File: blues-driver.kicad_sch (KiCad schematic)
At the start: 100 parts, among them Q5 LS844, Q6 BC858C, Q7 LS844, Q8 BC858C, Q9 BC848C, SW2 SW_DPDT_x2, SW3 SW_DIP_SPDT_2pos, U5 TLV9352, U6 TLV9352

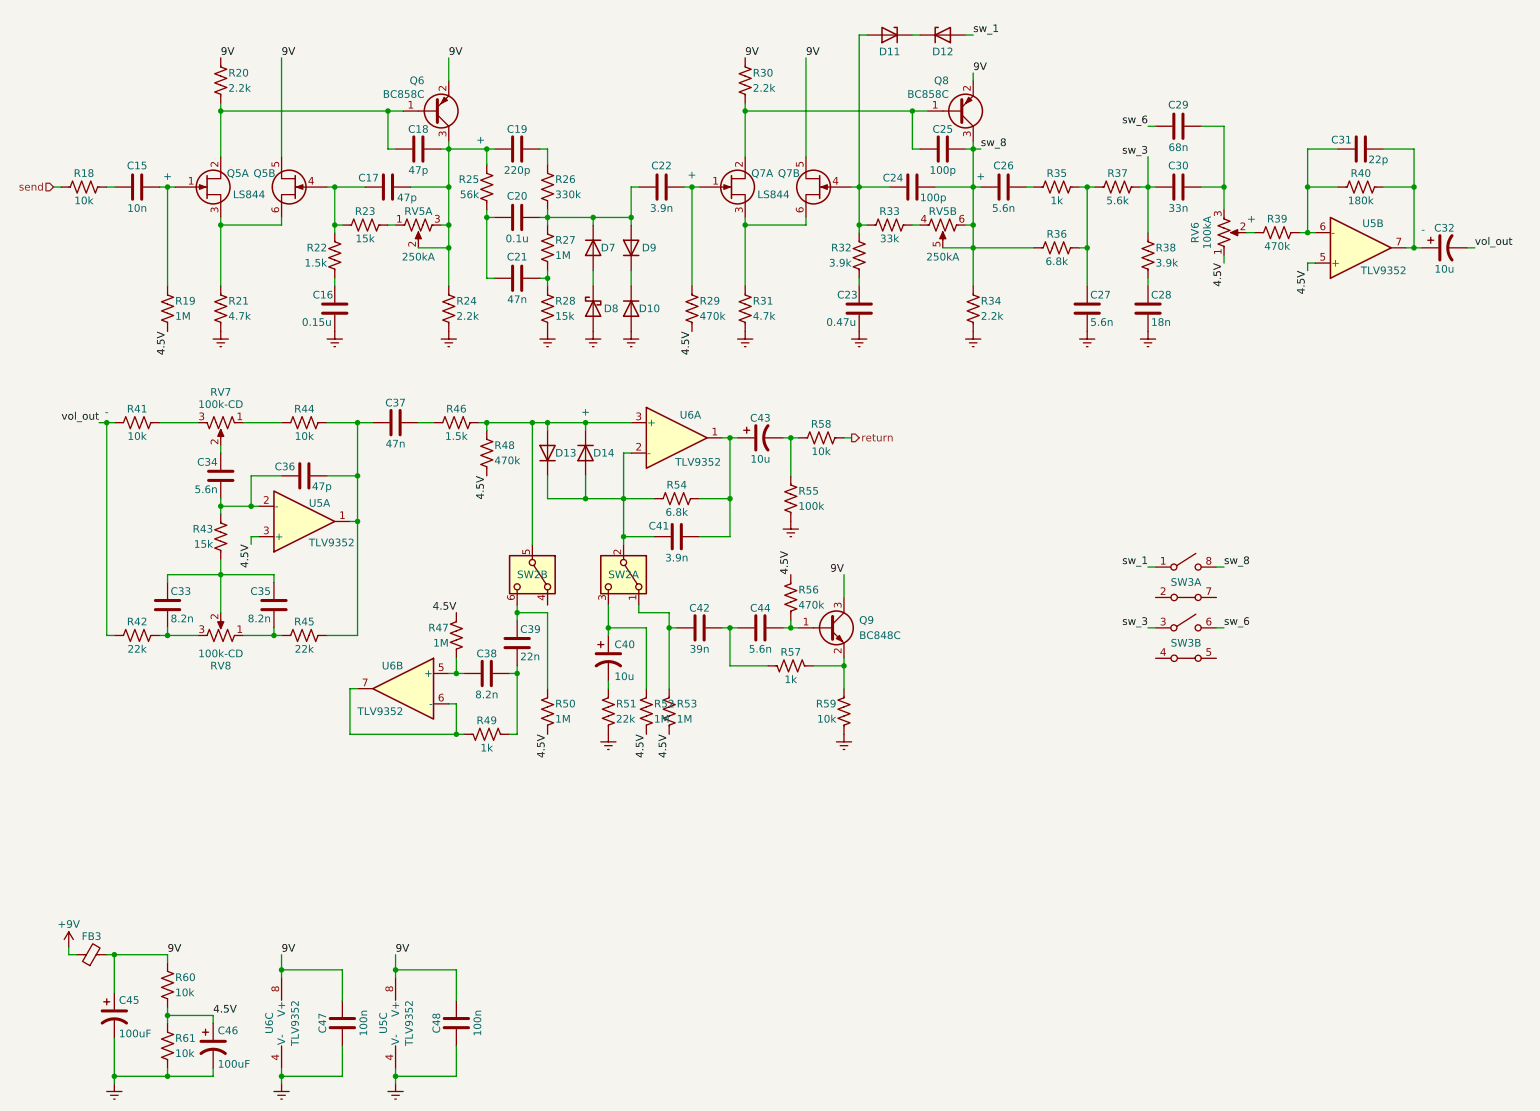
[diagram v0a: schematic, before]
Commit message: finished schematics, started PCB
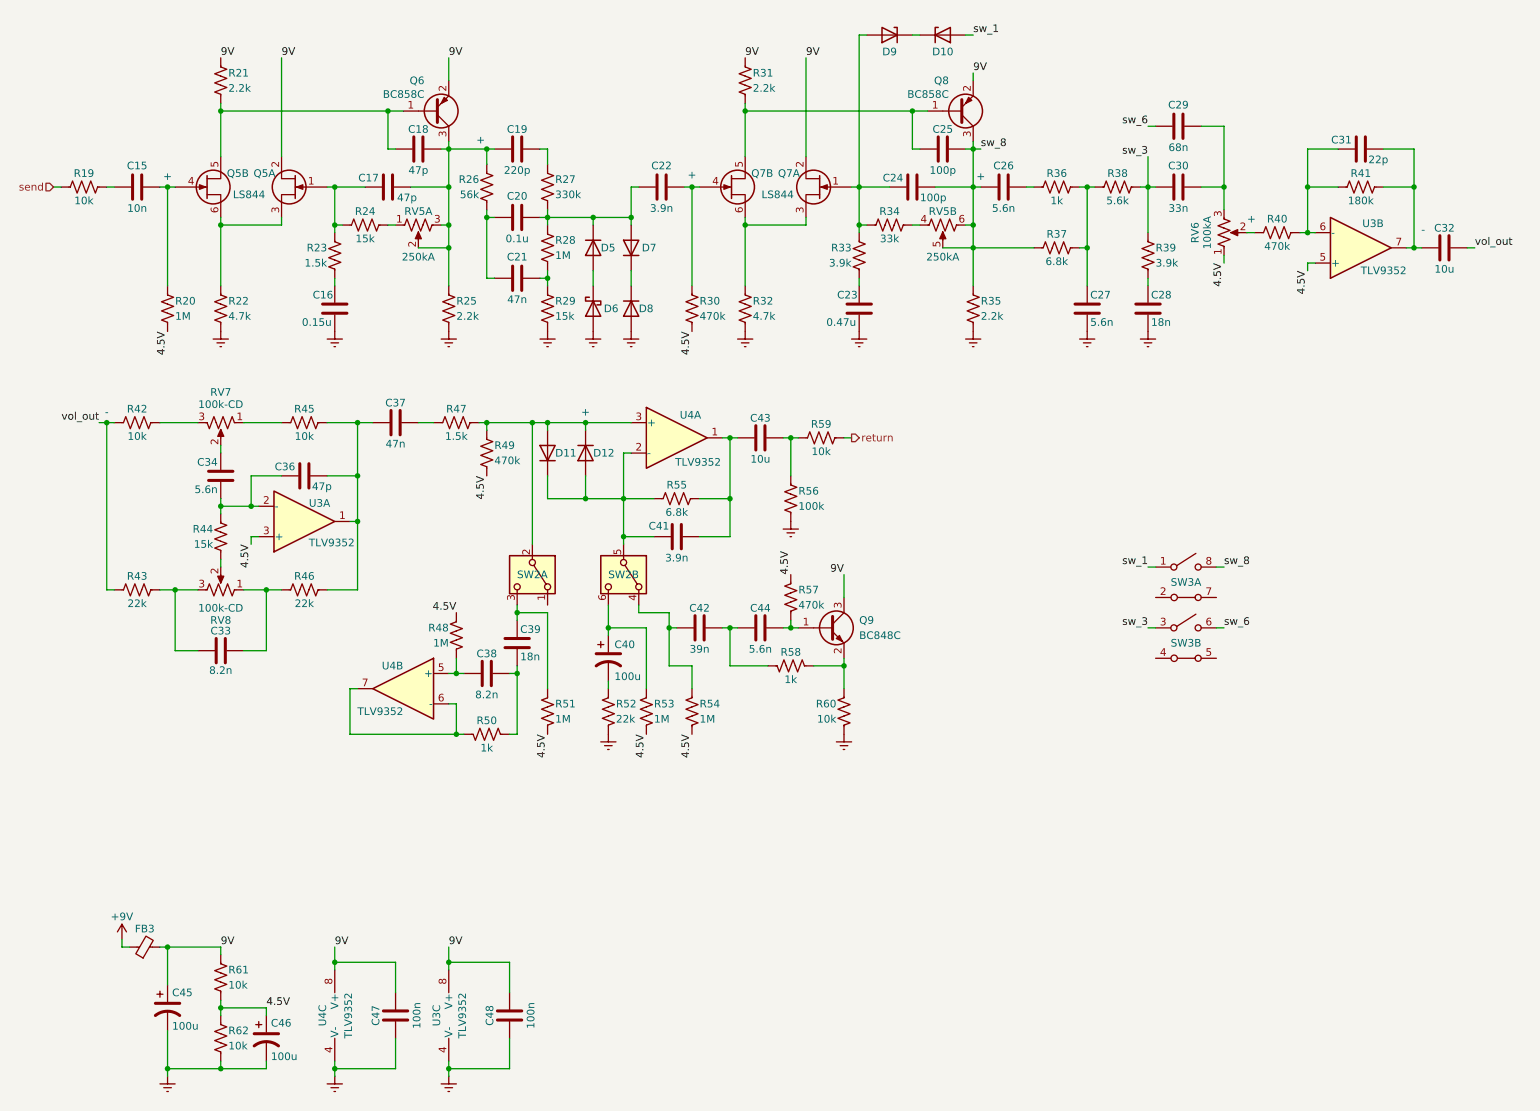
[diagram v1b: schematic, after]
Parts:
- removed C35: 8.2n, bca-footprints:C_Film_L7.2mm_W2.5mm_P5.00mm, symbol bca-symbols:C_Film_W2.50mm
- C17, C18, C24, C25, C31, C36, C47, C48: footprint bca-footprints:C_Ceramic_L4.0mm_W2.5mm_P2.50mm -> Capacitor_SMD:C_0805_2012Metric_Pad1.18x1.45mm_HandSolder
- C32, C43: footprint bca-footprints:CP_Radial_D4.0mm_P1.50mm -> Capacitor_SMD:C_0805_2012Metric_Pad1.18x1.45mm_HandSolder; symbol bca-symbols:CP_Audio -> bca-symbols:C_Ceramic
- C39: value 22n -> 18n
- C40: value 10u -> 100u; footprint bca-footprints:CP_Radial_D4.0mm_P1.50mm -> bca-footprints:CP_Radial_D6.3mm_P2.50mm; symbol bca-symbols:CP_Audio -> bca-symbols:CP_Power
- C45, C46: value 100uF -> 100u
- D10: renamed from D12; footprint (none) -> Diode_SMD:D_SOD-323_HandSoldering
- D11: renamed from D13; footprint (none) -> Diode_SMD:D_SOD-323_HandSoldering
- D12: renamed from D14; footprint (none) -> Diode_SMD:D_SOD-323_HandSoldering
- D5: renamed from D7; footprint (none) -> Diode_SMD:D_SOD-323_HandSoldering
- D6: renamed from D8; footprint (none) -> Diode_SMD:D_SOD-323_HandSoldering
- D7: renamed from D9; footprint (none) -> Diode_SMD:D_SOD-323_HandSoldering
- D8: renamed from D10; footprint (none) -> Diode_SMD:D_SOD-323_HandSoldering
- D9: renamed from D11; footprint (none) -> Diode_SMD:D_SOD-323_HandSoldering
- Q6, Q8, Q9: footprint (none) -> Package_TO_SOT_SMD:SOT-23_Handsoldering
- R20: renamed from R19; footprint bca-footprints:R_L3.6mm_D1.6mm_P5.00mm_Horizontal -> Resistor_SMD:R_0805_2012Metric_Pad1.20x1.40mm_HandSolder
- R21: renamed from R20; footprint bca-footprints:R_L3.6mm_D1.6mm_P5.00mm_Horizontal -> Resistor_SMD:R_0603_1608Metric_Pad0.98x0.95mm_HandSolder
- R22: renamed from R21; footprint bca-footprints:R_L3.6mm_D1.6mm_P5.00mm_Horizontal -> Resistor_SMD:R_0603_1608Metric_Pad0.98x0.95mm_HandSolder
- R25: renamed from R24; footprint bca-footprints:R_L3.6mm_D1.6mm_P5.00mm_Horizontal -> Resistor_SMD:R_0603_1608Metric_Pad0.98x0.95mm_HandSolder
- R31: renamed from R30; footprint bca-footprints:R_L3.6mm_D1.6mm_P5.00mm_Horizontal -> Resistor_SMD:R_0603_1608Metric_Pad0.98x0.95mm_HandSolder
- R32: renamed from R31; footprint bca-footprints:R_L3.6mm_D1.6mm_P5.00mm_Horizontal -> Resistor_SMD:R_0603_1608Metric_Pad0.98x0.95mm_HandSolder
- R35: renamed from R34; footprint bca-footprints:R_L3.6mm_D1.6mm_P5.00mm_Horizontal -> Resistor_SMD:R_0603_1608Metric_Pad0.98x0.95mm_HandSolder
- R48: renamed from R47; footprint bca-footprints:R_L3.6mm_D1.6mm_P5.00mm_Horizontal -> Resistor_SMD:R_0805_2012Metric_Pad1.20x1.40mm_HandSolder
- R51: renamed from R50; footprint bca-footprints:R_L3.6mm_D1.6mm_P5.00mm_Horizontal -> Resistor_SMD:R_0805_2012Metric_Pad1.20x1.40mm_HandSolder
- R53: renamed from R52; footprint bca-footprints:R_L3.6mm_D1.6mm_P5.00mm_Horizontal -> Resistor_SMD:R_0805_2012Metric_Pad1.20x1.40mm_HandSolder
- R54: renamed from R53; footprint bca-footprints:R_L3.6mm_D1.6mm_P5.00mm_Horizontal -> Resistor_SMD:R_0805_2012Metric_Pad1.20x1.40mm_HandSolder
- R61: renamed from R60; footprint bca-footprints:R_L3.6mm_D1.6mm_P5.00mm_Horizontal -> Resistor_SMD:R_0805_2012Metric_Pad1.20x1.40mm_HandSolder
- R62: renamed from R61; footprint bca-footprints:R_L3.6mm_D1.6mm_P5.00mm_Horizontal -> Resistor_SMD:R_0805_2012Metric_Pad1.20x1.40mm_HandSolder
- SW2: footprint (none) -> bca-footprints:SW_Toggle_DPDT_SolderLug
- SW3: footprint (none) -> bca-footprints:DIP-8_W7.62mm_Socket
- renumbered R18 to R19, R22 to R23, R23 to R24, R25 to R26, R26 to R27, R27 to R28, R28 to R29, R29 to R30, R32 to R33, R33 to R34, R35 to R36, R36 to R37, R37 to R38, R38 to R39, R39 to R40, R40 to R41, R41 to R42, R42 to R43, R43 to R44, R44 to R45, R45 to R46, R46 to R47, R48 to R49, R49 to R50, R51 to R52, R54 to R55, R55 to R56, R56 to R57, R57 to R58, R58 to R59, R59 to R60, U5 to U3, U6 to U4
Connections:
- net 9V: now also Q5.2 (D1), Q7.2 (D1); no longer Q5.5 (D2), Q7.5 (D2)
- net at C41.1, D11.1 (K), D12.2 (A)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: now also SW2.5 (B); no longer SW2.2 (B)
- net at D11.2 (A), D12.1 (K), R47.2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: now also SW2.2 (B); no longer SW2.5 (B)
- net at C17.1, R23.2, R24.1: now also Q5.1 (G1); no longer Q5.4 (G1)
- net at C25.1, Q8.1 (B), R31.1: now also Q7.5 (D2); no longer Q7.2 (D1)
- net at C24.1, D9.2 (A), R33.2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: now also Q7.1 (G1); no longer Q7.4 (G1)
- net at C42.1, R54.2: now also SW2.4 (A); no longer SW2.1 (A)
- net at C40.1, R53.2: now also SW2.6 (C); no longer SW2.3 (C)
- net at C15.2, R20.2: now also Q5.4 (G1); no longer Q5.1 (G1)
- net at R43.2, RV8.3: now also C33.2; no longer C33.1
- net at R46.1, RV8.1: now also C33.1
- net at R44.1, RV8.2: no longer C33.2
- net at C18.1, Q6.1 (B), R21.1: now also Q5.5 (D2); no longer Q5.2 (D1)
- net at C22.2, R30.2: now also Q7.4 (G1); no longer Q7.1 (G1)
- net at C39.2, R51.2: now also SW2.3 (C); no longer SW2.6 (C)
- new net: Q5.3 (S1), Q5.6 (S1), R22.2
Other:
- moved on the sheet: C33, C45, C46, C47, C48, FB3, Q7A, Q7B, R43, R46, R54, R61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

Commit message: initial layout
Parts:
- removed C37: 47n, bca-footprints:C_Film_L7.2mm_W2.5mm_P5.00mm, symbol bca-symbols:C_Film_W2.50mm
- removed C40: 100u, bca-footprints:CP_Radial_D6.3mm_P2.50mm, symbol bca-symbols:CP_Power
- removed R53: 1M, Resistor_SMD:R_0805_2012Metric_Pad1.20x1.40mm_HandSolder, symbol bca-symbols:R
- C17, C18, C24, C25, C31: footprint Capacitor_SMD:C_0805_2012Metric_Pad1.18x1.45mm_HandSolder -> Capacitor_SMD:C_0603_1608Metric_Pad1.08x0.95mm_HandSolder
- C23: value 0.47u -> 1u
- C35: renamed from C36; footprint Capacitor_SMD:C_0805_2012Metric_Pad1.18x1.45mm_HandSolder -> Capacitor_SMD:C_0603_1608Metric_Pad1.08x0.95mm_HandSolder
- C44: renamed from C47; footprint Capacitor_SMD:C_0805_2012Metric_Pad1.18x1.45mm_HandSolder -> Capacitor_SMD:C_0603_1608Metric_Pad1.08x0.95mm_HandSolder
- C45: renamed from C48; footprint Capacitor_SMD:C_0805_2012Metric_Pad1.18x1.45mm_HandSolder -> Capacitor_SMD:C_0603_1608Metric_Pad1.08x0.95mm_HandSolder
- D10: value 3v3 Zener -> 4v7 Zener
- R52: value 22k -> 33k; footprint bca-footprints:R_L3.6mm_D1.6mm_P5.00mm_Horizontal -> Resistor_SMD:R_0805_2012Metric_Pad1.20x1.40mm_HandSolder
- renumbered C34 to C33, C33 to C34, C38 to C36, C39 to C37, C42 to C38, C41 to C39, C44 to C40, C43 to C41, C45 to C42, C46 to C43, R49 to R48, R48 to R49, R54 to R53, R55 to R54, R57 to R55, R58 to R56, R56 to R57, R60 to R58, R61 to R60, R62 to R61
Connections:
- net 4.5V: now also R52.1
- net Earth: no longer R52.1
- net at C39.1, D11.1 (K), D12.2 (A)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: now also SW2.2 (B); no longer SW2.5 (B)
- net at D11.2 (A), D12.1 (K), R47.2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: now also SW2.5 (B); no longer SW2.2 (B)
- net at C38.1, R53.2: now also SW2.1 (A); no longer SW2.4 (A)
- net at SW2.6 (C): now also C37.2, R51.2
- net at R52.2: now also SW2.4 (A)
- net at R47.1: now also C35.2, R45.2, R46.2, U3.1
- now unconnected: SW2.3 (C)
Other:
- moved on the sheet: C38, C40, C42, C43, C44, C45, FB3, Q9, R47, R48, R53, R55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

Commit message: first draft PCB
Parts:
- C15: value 10n -> 18n
- C31: value 22p -> 47p
- C32, C41: footprint Capacitor_SMD:C_0805_2012Metric_Pad1.18x1.45mm_HandSolder -> Capacitor_SMD:C_1206_3216Metric_Pad1.33x1.80mm_HandSolder; JLCPCB PART # (none) -> C13585
- C33: value 5.6n -> 3.9n
- C34: value 8.2n -> 15n
- C37: value 18n -> 15n
- C38: value 39n -> 33n
- D10: value 4v7 Zener -> 4v7 Z; footprint Diode_SMD:D_SOD-323_HandSoldering -> bca-footprints:Diode_Zener_DO-35_P5.00mm
- D11, D12, D5, D6, D7, D8: footprint Diode_SMD:D_SOD-323_HandSoldering -> bca-footprints:Diode_DO-35_P5.00mm
- D9: value 3v3 Zener -> 3v3 Z; footprint Diode_SMD:D_SOD-323_HandSoldering -> bca-footprints:Diode_Zener_DO-35_P5.00mm
- R33: value 3.9k -> 2.2k
- R34: value 33k -> 22k
- R42, R45: value 10k -> 15k
- R44: value 15k -> 10k
- R47: value 1.5k -> 6.8k
- R53: value 1M -> 56k; footprint Resistor_SMD:R_0805_2012Metric_Pad1.20x1.40mm_HandSolder -> bca-footprints:R_L3.6mm_D1.6mm_P5.00mm_Horizontal
- R56: value 1k -> 1.5k
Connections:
- net 9V: now also Q7.5 (D2); no longer Q7.2 (D1)
- net at C25.1, Q8.1 (B), R31.1: now also Q7.2 (D1); no longer Q7.5 (D2)
- net at C24.1, D9.2 (A), R33.2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: now also Q7.4 (G1); no longer Q7.1 (G1)
- net at SW2.4 (A): no longer R52.2
- net at C22.2, R30.2: now also Q7.1 (G1); no longer Q7.4 (G1)
- net at SW2.3 (C): now also R52.2
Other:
- moved on the sheet: Q7A, Q7B, R52, SW2B

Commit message: generated production files
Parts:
- C15, C28: value 18n -> 18nF
- C16: value 0.15u -> 0.15uF
- C17, C18, C31, C35: value 47p -> 47pF
- C19: value 220p -> 220pF
- C20: value 0.1u -> 0.1uF
- C21: value 47n -> 47nF
- C22, C33, C39: value 3.9n -> 3.9nF
- C23: value 1u -> 1uF
- C24, C25: value 100p -> 100pF
- C26, C27, C40: value 5.6n -> 5.6nF
- C29: value 68n -> 68nF
- C30, C38: value 33n -> 33nF
- C32, C41: value 10u -> 10uF; footprint Capacitor_SMD:C_1206_3216Metric_Pad1.33x1.80mm_HandSolder -> bca-footprints:CP_Radial_D4.0mm_P1.50mm; symbol bca-symbols:C_Ceramic -> bca-symbols:CP_Audio; JLCPCB PART # C13585 -> (none)
- C34, C37: value 15n -> 15nF
- C36: value 8.2n -> 8.2nF
- C42, C43: value 100u -> 100uF
- C44, C45: value 100n -> 100nF
- D10: value 4v7 Z -> 4v7 Zener
- D9: value 3v3 Z -> 3v3 Zener
- Q6, Q8: value BC858C -> BC857C
- Q9: value BC848C -> BC847C
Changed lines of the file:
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@@
 			)
 		)
-		(property "Value" "100p"
+		(property "Value" "100pF"
 			(at 163.83 44.958 90)
 			(effects
@@
 			)
 		)
-		(property "Value" "47p"
+		(property "Value" "47pF"
 			(at 76.454 44.958 90)
 			(effects
@@
 			)
 		)
-		(property "Value" "100n"
+		(property "Value" "100nF"
 			(at 73.406 181.61 90)
 			(effects
@@
 			)
 		)
-		(property "Value" "18n"
+		(property "Value" "18nF"
 			(at 33.02 46.736 90)
 			(effects
@@
 			)
 		)
-		(property "Value" "47n"
+		(property "Value" "47nF"
 			(at 96.52 61.976 90)
 			(effects
@@
 			)
 		)
-		(property "Value" "3v3 Z"
+		(property "Value" "3v3 Zener"
 			(at 158.75 20.574 0)
 			(effects
@@
 			)
 		)
-		(property "Value" "18n"
+		(property "Value" "18nF"
 			(at 202.438 65.786 0)
 			(effects
@@
 	)
 	(symbol
-		(lib_id "bca-symbols:C_Ceramic")
+		(lib_id "bca-symbols:CP_Audio")
 		(at 137.16 85.09 90)
 		(mirror x)
@@
 			)
 		)
-		(property "Value" "10u"
+		(property "Value" "10uF"
 			(at 137.16 88.646 90)
 			(effects
@@
 			)
 		)
-		(property "Footprint" "Capacitor_SMD:C_1206_3216Metric_Pad1.33x1.80mm_HandSolder"
-			(at 140.97 86.0552 0)
+		(property "Footprint" "bca-footprints:CP_Radial_D4.0mm_P1.50mm"
+			(at 147.32 85.09 0)
 			(effects
 				(font
@@
 			)
 		)
-		(property "Description" "Unpolarized capacitor"
+		(property "Description" "Polarized capacitor, footprint sized for power rails"
 			(at 137.16 85.09 0)
 			(effects
@@
 			)
 		)
-		(property "JLCPCB PART #" "C13585"
+		(property "JLCPCB PART #" ""
 			(at 137.16 85.09 90)
 			(effects
@@
 			)
 		)
-		(property "Value" "220p"
+		(property "Value" "220pF"
 			(at 96.52 40.386 90)
 			(effects
@@
 			)
 		)
-		(property "Value" "47p"
+		(property "Value" "47pF"
 			(at 80.01 40.386 90)
 			(effects
@@
 			)
 		)
-		(property "Value" "15n"
+		(property "Value" "15nF"
 			(at 46.99 123.952 90)
 			(effects
@@
 			)
 		)
-		(property "Value" "5.6n"
+		(property "Value" "5.6nF"
 			(at 192.278 65.786 0)
 			(effects
@@
 			)
 		)
-		(property "Value" "4v7 Z"
+		(property "Value" "4v7 Zener"
 			(at 167.64 20.574 0)
 			(effects
@@
 			)
 		)
-		(property "Value" "BC848C"
+		(property "Value" "BC847C"
 			(at 148.59 118.1099 0)
 			(effects
@@
 			)
 		)
-		(property "Value" "100p"
+		(property "Value" "100pF"
 			(at 167.64 40.386 90)
 			(effects
@@
 			)
 		)
-		(property "Value" "8.2n"
+		(property "Value" "8.2nF"
 			(at 91.44 128.016 90)
 			(effects
@@
 			)
 		)
-		(property "Value" "100u"
+		(property "Value" "100uF"
 			(at 49.022 188.468 0)
 			(effects
@@
 	)
 	(symbol
-		(lib_id "bca-symbols:C_Ceramic")
+		(lib_id "bca-symbols:CP_Audio")
 		(at 251.46 53.34 90)
 		(mirror x)
@@
 			)
 		)
-		(property "Value" "10u"
+		(property "Value" "10uF"
 			(at 251.46 56.896 90)
 			(effects
@@
 			)
 		)
-		(property "Footprint" "Capacitor_SMD:C_1206_3216Metric_Pad1.33x1.80mm_HandSolder"
-			(at 255.27 54.3052 0)
+		(property "Footprint" "bca-footprints:CP_Radial_D4.0mm_P1.50mm"
+			(at 261.62 53.34 0)
 			(effects
 				(font
@@
 			)
 		)
-		(property "Description" "Unpolarized capacitor"
+		(property "Description" "Polarized capacitor, footprint sized for power rails"
 			(at 251.46 53.34 0)
 			(effects
@@
 			)
 		)
-		(property "JLCPCB PART #" "C13585"
+		(property "JLCPCB PART #" ""
 			(at 251.46 53.34 90)
 			(effects
@@
 			)
 		)
-		(property "Value" "47p"
+		(property "Value" "47pF"
 			(at 62.23 93.218 90)
 			(effects
@@
 			)
 		)
-		(property "Value" "100n"
+		(property "Value" "100nF"
 			(at 92.456 181.61 90)
 			(effects
@@
 			)
 		)
-		(property "Value" "33n"
+		(property "Value" "33nF"
 			(at 121.92 120.396 90)
 			(effects
@@
 			)
 		)
-		(property "Value" "1u"
+		(property "Value" "1uF"
 			(at 153.162 65.786 0)
 			(effects
@@
 			)
 		)
-		(property "Value" "3.9n"
+		(property "Value" "3.9nF"
 			(at 120.65 46.736 90)
 			(effects
@@
 			)
 		)
-		(property "Value" "BC858C"
+		(property "Value" "BC857C"
 			(at 81.026 27.686 0)
 			(effects
@@
 			)
 		)
-		(property "Value" "47p"
+		(property "Value" "47pF"
 			(at 239.014 38.608 90)
 			(effects
@@
 			)
 		)
-		(property "Value" "BC858C"
+		(property "Value" "BC857C"
 			(at 168.656 27.686 0)
 			(effects
@@
 			)
 		)
-		(property "Value" "5.6n"
+		(property "Value" "5.6nF"
 			(at 177.8 46.736 90)
 			(effects
@@
 			)
 		)
-		(property "Value" "68n"
+		(property "Value" "68nF"
 			(at 207.01 36.576 90)
 			(effects
@@
 			)
 		)
-		(property "Value" "5.6n"
+		(property "Value" "5.6nF"
 			(at 132.08 120.396 90)
 			(effects
@@
 			)
 		)
-		(property "Value" "3.9n"
+		(property "Value" "3.9nF"
 			(at 123.19 105.156 90)
 			(effects
@@
 			)
 		)
-		(property "Value" "3.9n"
+		(property "Value" "3.9nF"
 			(at 46.482 93.726 0)
 			(effects
@@
 			)
 		)
-		(property "Value" "0.1u"
+		(property "Value" "0.1uF"
 			(at 96.52 51.816 90)
 			(effects
@@
 			)
 		)
-		(property "Value" "100u"
+		(property "Value" "100uF"
 			(at 32.512 183.388 0)
 			(effects
@@
 			)
 		)
-		(property "Value" "33n"
+		(property "Value" "33nF"
 			(at 207.01 46.736 90)
 			(effects
@@
 			)
 		)
-		(property "Value" "15n"
+		(property "Value" "15nF"
 			(at 97.028 121.666 0)
 			(effects
@@
 			)
 		)
-		(property "Value" "0.15u"
+		(property "Value" "0.15uF"
 			(at 65.532 65.786 0)
 			(effects

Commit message: re-generated gerbers, finalized BOM
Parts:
- R33: value 2.2k -> 3.9k
- R54: value 6.8k -> 5.6k
